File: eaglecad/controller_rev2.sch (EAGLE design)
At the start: 108 parts, among them J1 1.27MM-SWD-CONNECTOR, U100 STM32F042K6, U101 TCAN330, U200 TPS63070, U300 STSPIN230, U301 TSV991ILT, U302 AS5047P, U400 STSPIN250, U401 TSV991ILT, X101 16MHZ-2.5x2mm

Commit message: progress on layout
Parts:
- removed C304: 1n, rcl_custom:C-EU0402-B-NOSILK
- removed JP301: (no value), adafruit:PINHD-1X3
- removed R301: 18k, rcl_custom:R-US_0402-B-NOSILK
- added JP1: (no value), pinhead:PINHD-1X3
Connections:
- removed net PA15/SPI1_NSS: U100.PA15, U302.CSN
- removed net PA6/CAN_LSTN: U100.PA6, U101.S
- new net PA15/CAN_LSTN: U100.PA15, U101.S
- new net PA6/SPI1_NSS: U100.PA6, U302.CSN
- net 3.3V: no longer R301.2
- net GND: no longer C304.1
- net STBY/RESET_BLDC: no longer C304.2, R301.1
- net U: now also JP1.1; no longer JP301.1
- net V: now also JP1.2; no longer JP301.2
- net W: now also JP1.3; no longer JP301.3

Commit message: [WIP] restore from workstation @E-Ruhl
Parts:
- removed TP102: TEST-POINT, Tova:TEST-POINT
- added BOOT1: TPTP15SQ, testpad:TPTP15SQ
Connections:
- net N$12 renamed TSP-FB2
- net N$9 renamed TSP-VSEL
- net CAN_SHDN: now also BOOT1.TP; no longer TP102.1
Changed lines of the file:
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@@
 <part name="GND2" library="supply1" library_urn="urn:adsk.eagle:library:371" deviceset="GND" device=""/>
 <part name="U300" library="U-ST-STSPIN230-BLDC-controller" deviceset="STSPIN230" device=""/>
-<part name="TP102" library="Tova" deviceset="TEST-POINT" device=""/>
 <part name="JP401" library="pinhead" library_urn="urn:adsk.eagle:library:325" deviceset="PINHD-1X2" device="" package3d_urn="urn:adsk.eagle:package:22435/2"/>
 <part name="U302" library="U-AMS-AS5047P-encoder" deviceset="AS5047P" device=""/>
@@
 <part name="LED_V_BATT" library="led" library_urn="urn:adsk.eagle:library:259" deviceset="LED" device="CHIPLED_0603" package3d_urn="urn:adsk.eagle:package:15822/2"/>
 <part name="JP1" library="pinhead" library_urn="urn:adsk.eagle:library:325" deviceset="PINHD-1X3" device="" package3d_urn="urn:adsk.eagle:package:22458/2"/>
+<part name="BOOT1" library="testpad" library_urn="urn:adsk.eagle:library:385" deviceset="TP" device="TP15SQ" package3d_urn="urn:adsk.eagle:package:27975/1"/>
 </parts>
 <sheets>
@@
 <instance part="SUPPLY2" gate="G$1" x="91.44" y="116.84"/>
 <instance part="GND3" gate="1" x="91.44" y="100.33" rot="MR0"/>
-<instance part="TP102" gate="G$1" x="142.24" y="106.68" smashed="yes" rot="MR0">
-<attribute name="NAME" x="139.7" y="104.14" size="1.778" layer="95" font="vector" rot="MR0"/>
-</instance>
 <instance part="C203" gate="CE" x="186.69" y="219.71" smashed="yes">
 <attribute name="DIS" x="186.69" y="219.71" size="1.778" layer="96" display="off"/>
@@
 <attribute name="NAME" x="140.716" y="208.788" size="1.778" layer="95" rot="R90"/>
 <attribute name="VALUE" x="142.875" y="213.868" size="1.778" layer="96" rot="R90"/>
+</instance>
+<instance part="BOOT1" gate="G$1" x="142.24" y="109.22" smashed="yes">
+<attribute name="TP_SIGNAL_NAME" x="143.51" y="107.95" size="1.778" layer="97"/>
 </instance>
 </instances>
@@
 <pinref part="U101" gate="G$1" pin="SHDN"/>
 <label x="142.24" y="106.68" size="1.778" layer="95" xref="yes"/>
-<pinref part="TP102" gate="G$1" pin="1"/>
 <wire x1="142.24" y1="106.68" x2="129.54" y2="106.68" width="0.1524" layer="91"/>
+<pinref part="BOOT1" gate="G$1" pin="TP"/>
 </segment>
 </net>
@@
 </segment>
 </net>
-<net name="N$9" class="0">
+<net name="TSP-VSEL" class="0">
 <segment>
 <pinref part="VSEL" gate="G$1" pin="TP"/>
@@
 </segment>
 </net>
-<net name="N$12" class="0">
+<net name="TSP-FB2" class="0">
 <segment>
 <pinref part="U200" gate="G$1" pin="FB2"/>

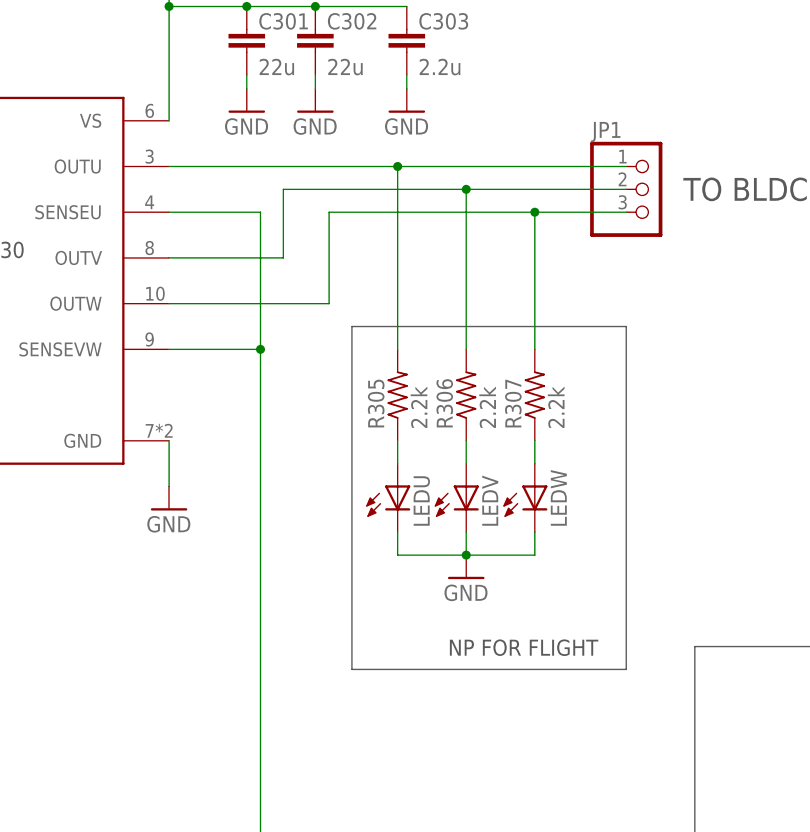
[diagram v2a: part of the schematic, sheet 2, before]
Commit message: Rev 2 minus thermals and JTAG
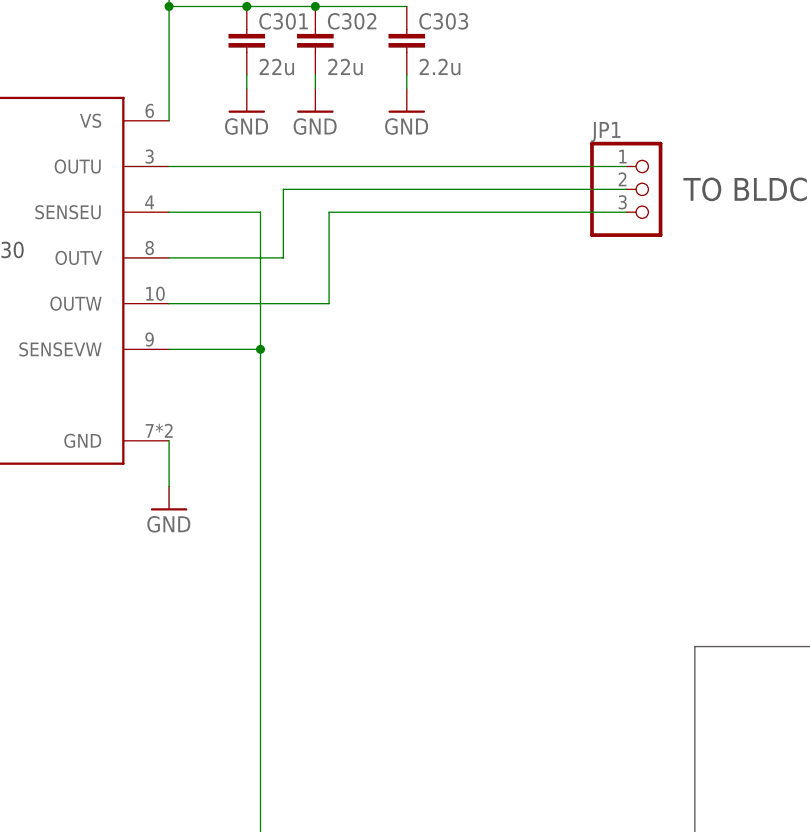
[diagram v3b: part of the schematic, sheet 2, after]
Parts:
- removed LED+, LED-, LEDU, LEDV, LEDW: (no value), adafruit:LEDCHIP-LED0603
- removed LED_V_BATT: (no value), led:LEDCHIPLED_0603
- removed R1, R2: 0, rcl_custom:R-US_0805-B-NOSILK
- removed R305, R306, R307, R411, R412: 2.2k, oresat-rcl:R-US_0805-B-NOSILK
- added R208: 2.2k, oresat-rcl:R-US_0603-B-NOSILK
- R206: value 100k -> 150k
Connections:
- removed net N$10: LEDV.A, R306.1
- removed net N$11: LEDW.A, R307.1
- removed net N$18: LED_V_BATT.A, R1.1
- removed net N$22: LED+.A, R411.1
- removed net N$23: LED-.A, R412.2
- removed net N$6: LEDU.A, R305.1
- net 3.3V: now also R208.2; no longer R2.2
- net GND: no longer LED+.C, LED-.C, LEDU.C, LEDV.C, LEDW.C, LED_V_BATT.C
- net N$20: now also R208.1; no longer R2.1
- net OUT1: no longer R411.2
- net OUT2: no longer R412.1
- net U: no longer R305.2
- net V: no longer R306.2
- net V_BATT: no longer R1.2
- net W: no longer R307.2

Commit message: rev2 LFD
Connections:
- net PA15/CAN_LSTN renamed PA15/CAN_SILENT
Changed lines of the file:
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@@
 <wire x1="185.42" y1="127" x2="185.42" y2="63.5" width="0.1524" layer="91"/>
 <label x="211.836" y="127" size="1.778" layer="95" rot="MR0"/>
-<label x="162.56" y="60.96" size="1.778" layer="95"/>
+<label x="162.56" y="63.5" size="1.778" layer="95"/>
 <pinref part="JP102" gate="G$1" pin="TXO"/>
 <wire x1="185.42" y1="63.5" x2="154.94" y2="63.5" width="0.1524" layer="91"/>
@@
 <wire x1="215.9" y1="124.46" x2="187.96" y2="124.46" width="0.1524" layer="91"/>
 <label x="212.344" y="124.46" size="1.778" layer="95" rot="MR0"/>
-<label x="162.56" y="63.5" size="1.778" layer="95"/>
+<label x="162.56" y="60.96" size="1.778" layer="95"/>
 <pinref part="JP102" gate="G$1" pin="RXI"/>
 <wire x1="187.96" y1="60.96" x2="154.94" y2="60.96" width="0.1524" layer="91"/>
@@
 </segment>
 </net>
-<net name="PA15/CAN_LSTN" class="0">
+<net name="PA15/CAN_SILENT" class="0">
 <segment>
 <pinref part="U101" gate="G$1" pin="S"/>
